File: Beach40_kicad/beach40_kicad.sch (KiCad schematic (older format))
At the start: 9 parts, among them T1 TRANSFO

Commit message: Some tinkering.
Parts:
- removed SMA_E1: RF IN, symbol SMA_EDGE
- added J1: SMA, SMA, symbol SMA
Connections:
- wire segments 22 -> 18
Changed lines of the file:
@@
 EESchema Schematic File Version 2
+LIBS:sma
 LIBS:power
 LIBS:device
@@
 LIBS:contrib
 LIBS:valves
-LIBS:sma_edge
 LIBS:beach40_kicad-cache
-EELAYER 25 0
+EELAYER 27 0
 EELAYER END
 $Descr A4 11693 8268
@@
 Sheet 1 1
 Title ""
-Date "19 jan 2015"
+Date "27 jan 2015"
 Rev ""
 Comp ""
@@
 Comment4 ""
 $EndDescr
-$Comp
-L SMA_EDGE SMA_E1
-U 1 1 54BB5708
-P 1650 5000
-F 0 "SMA_E1" H 1800 5300 60  0000 C CNN
-F 1 "RF IN" H 1800 5200 60  0000 C CNN
-F 2 "" H 1650 5000 60  0000 C CNN
-F 3 "" H 1650 5000 60  0000 C CNN
-	1    1650 5000
-	-1   0    0    1
-$EndComp
 $Comp
 L POT RV1
@@
 $EndComp
 Wire Wire Line
-	2000 5000 2100 5000
-Wire Wire Line
 	2500 5000 2650 5000
 $Comp
-L GND #PWR03
-U 1 1 54C61B84
-P 2100 5450
-F 0 "#PWR03" H 2100 5450 30  0001 C CNN
-F 1 "GND" H 2100 5380 30  0001 C CNN
-F 2 "" H 2100 5450 60  0000 C CNN
-F 3 "" H 2100 5450 60  0000 C CNN
-	1    2100 5450
-	1    0    0    -1
-$EndComp
-$Comp
-L GND #PWR04
-U 1 1 54C61BBC
-P 2050 4550
-F 0 "#PWR04" H 2050 4550 30  0001 C CNN
-F 1 "GND" H 2050 4480 30  0001 C CNN
-F 2 "" H 2050 4550 60  0000 C CNN
-F 3 "" H 2050 4550 60  0000 C CNN
-	1    2050 4550
-	1    0    0    -1
-$EndComp
-Wire Wire Line
-	2000 5100 2000 5450
-Wire Wire Line
-	2000 5450 2100 5450
-Wire Wire Line
-	2000 4900 2000 4550
-Wire Wire Line
-	2000 4550 2050 4550
+L SMA J1
+U 1 1 54C729C5
+P 1750 5300
+F 0 "J1" H 1875 5615 60  0000 C CNN
+F 1 "SMA" H 1940 5540 60  0000 C CNN
+F 2 "SMA" H 1925 5470 50  0000 C CNN
+F 3 "" H 1750 5300 60  0000 C CNN
+	1    1750 5300
+	-1   0    0    -1
+$EndComp
+Wire Wire Line
+	1900 5000 2100 5000
 $EndSCHEMATC

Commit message: 2 RF amp stages, first attempt at layout, 1206 for the most part.
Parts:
- removed C1: 10nF, symbol C
- removed RV1: 200, ~, symbol POT
- added C1: 10n, FT:1210_CAP, symbol CAP
- added C3, C5, C6, C7, C8, C9: 100n, FT:1210_CAP, symbol CAP
- added C4: 1n, FT:1210_CAP, symbol CAP
- added L1: 10T BiFilar, FT:IND_SRP1040, symbol INDUCTOR
- added L2, L3, L4: 10t BiFilar, FT:IND_SRP1040, symbol INDUCTOR
- added Q1: 2N2222, FT:SOT23_TRANSISTOR, symbol TRANSISTOR_NPN
- added Q2: BD139, FT:SOT23_TRANSISTOR, symbol TRANSISTOR_NPN
- added R1, R4: 100, FT:1206, symbol R
- added R2, R7: 2.2k, FT:1206, symbol R
- added R3: 1k1, FT:1206, symbol R
- added R5: 10, FT:1206, symbol R
- added R6: 470, FT:1206, symbol R
- added R8: 22, FT:1206, symbol R
- added R9: 4.7, FT:1206, symbol R
- added VR1: 200, FT:POT_TRIM_PTH, symbol POT
- 4:1: renamed from T1; symbol TRANSFO -> TRANSFORMER
- C2: footprint (none) -> FT:1210_CAP; symbol C -> CAP
- D1, D2, D3, D4: footprint ~ -> FT:1206_DIODE
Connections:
- net labels added: +12V, LPF
- wire segments 18 -> 63

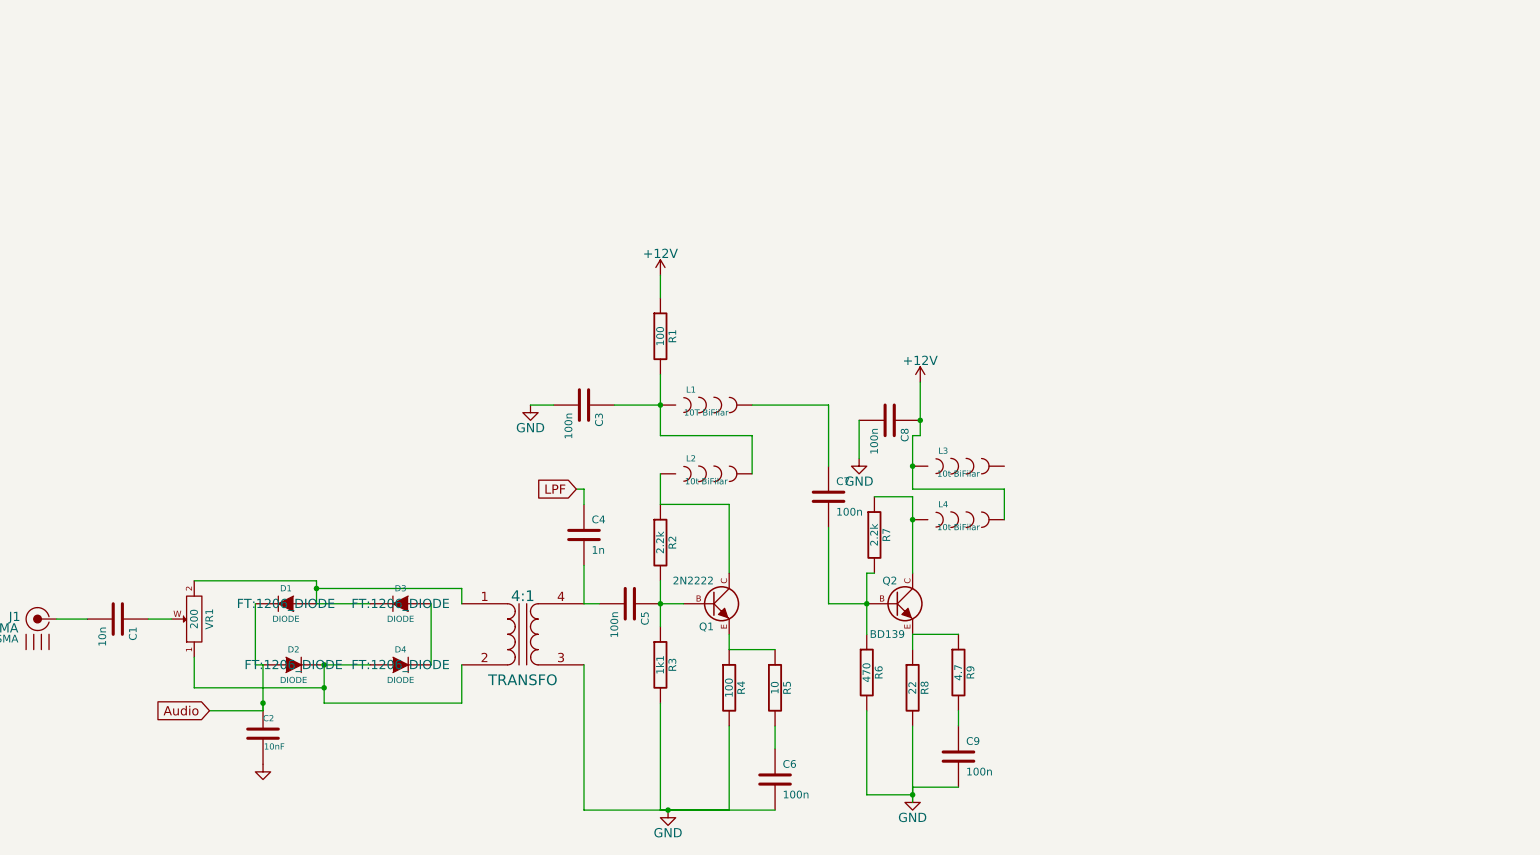
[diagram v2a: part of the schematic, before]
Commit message: - more work! transmit RF path finish.
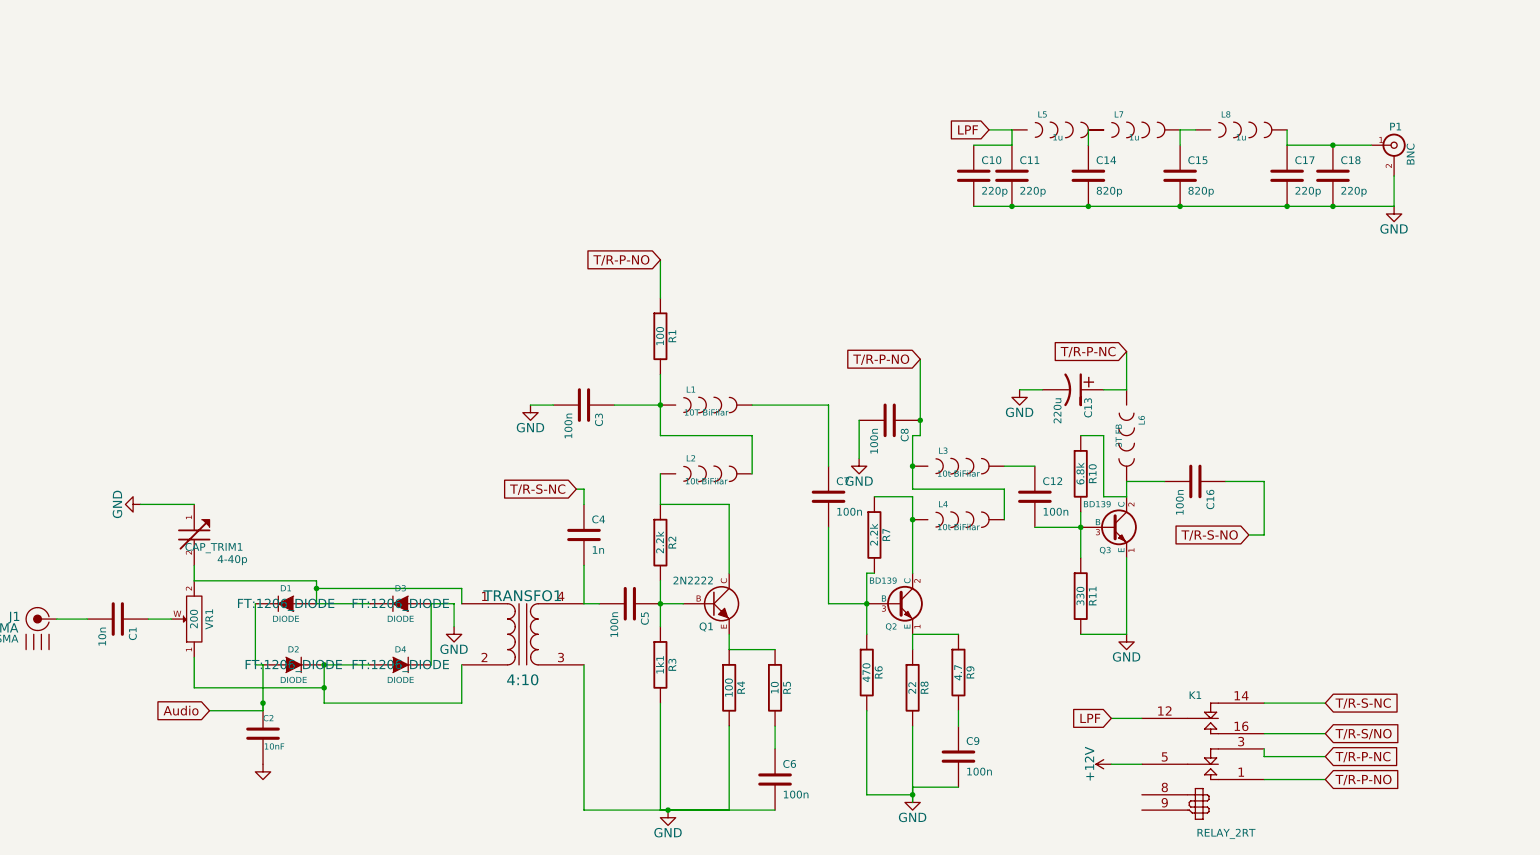
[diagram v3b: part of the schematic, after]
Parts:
- removed Q2: BD139, FT:SOT23_TRANSISTOR, symbol TRANSISTOR_NPN
- added C10, C11, C17, C18: 220p, symbol CAP
- added C12, C16: 100n, symbol CAP
- added C13: 220u, symbol C_POL
- added C14, C15: 820p, symbol CAP
- added CAP_TRIM1: 4-40p, symbol CAP_TRIM
- added K1: RELAY_2RT, symbol RELAY_2RT
- added L5, L7, L8: 1u, symbol INDUCTOR
- added L6: 3T FB, symbol INDUCTOR
- added P1: BNC, symbol BNC
- added Q2: BD139, FT:SOT23_TRANSISTOR, symbol BD139
- added Q3: BD139, TO126, symbol BD139
- added R10: 6.8k, symbol R
- added R11: 330, symbol R
- TRANSFO1: renamed from 4:1; value TRANSFO -> 4:10
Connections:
- net +12V: now also K1.5 (C1); no longer C8.1, L3.1, L4.2, R1.1
- net GND: now also D3.A, D4.K, C10.2, C11.2, C13.2 (-), C14.2, C15.2, C17.2, C18.2, CAP_TRIM1.1, P1.2 (Ext), Q3.1 (E), R11.2
- net LPF: now also C10.1, C11.1, K1.12 (C2), L5.1; no longer C4.1
- net at D1.A, D3.K, TRANSFO1.1 (AA)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: now also CAP_TRIM1.2
- net at C7.2, R6.1, R7.2: now also Q2.3 (B)
- net at L4.1, R7.1: now also Q2.2 (C)
- net at R8.1, R9.1: now also Q2.1 (E)
- net at L3.2: now also C12.1
- new net: C12.2, Q3.3 (B), R10.2, R11.1
- new net: C16.2, L6.2, Q3.2 (C), R10.1
- new net: C14.1, L7.1
- new net: C15.1, L7.2, L8.1
- new net: C17.1, C18.1, L8.2, P1.1 (In)
- new net T/R-P-NC: C13.1 (+), K1.3 (R1), L6.1
- new net T/R-P-NO: C8.1, K1.1 (T1), L3.1, L4.2, R1.1
- new net T/R-S-NC: C4.1, K1.14 (R2)
- new net T/R-S-NO: C16.1
- new net T/R-S/NO: K1.16 (T2)

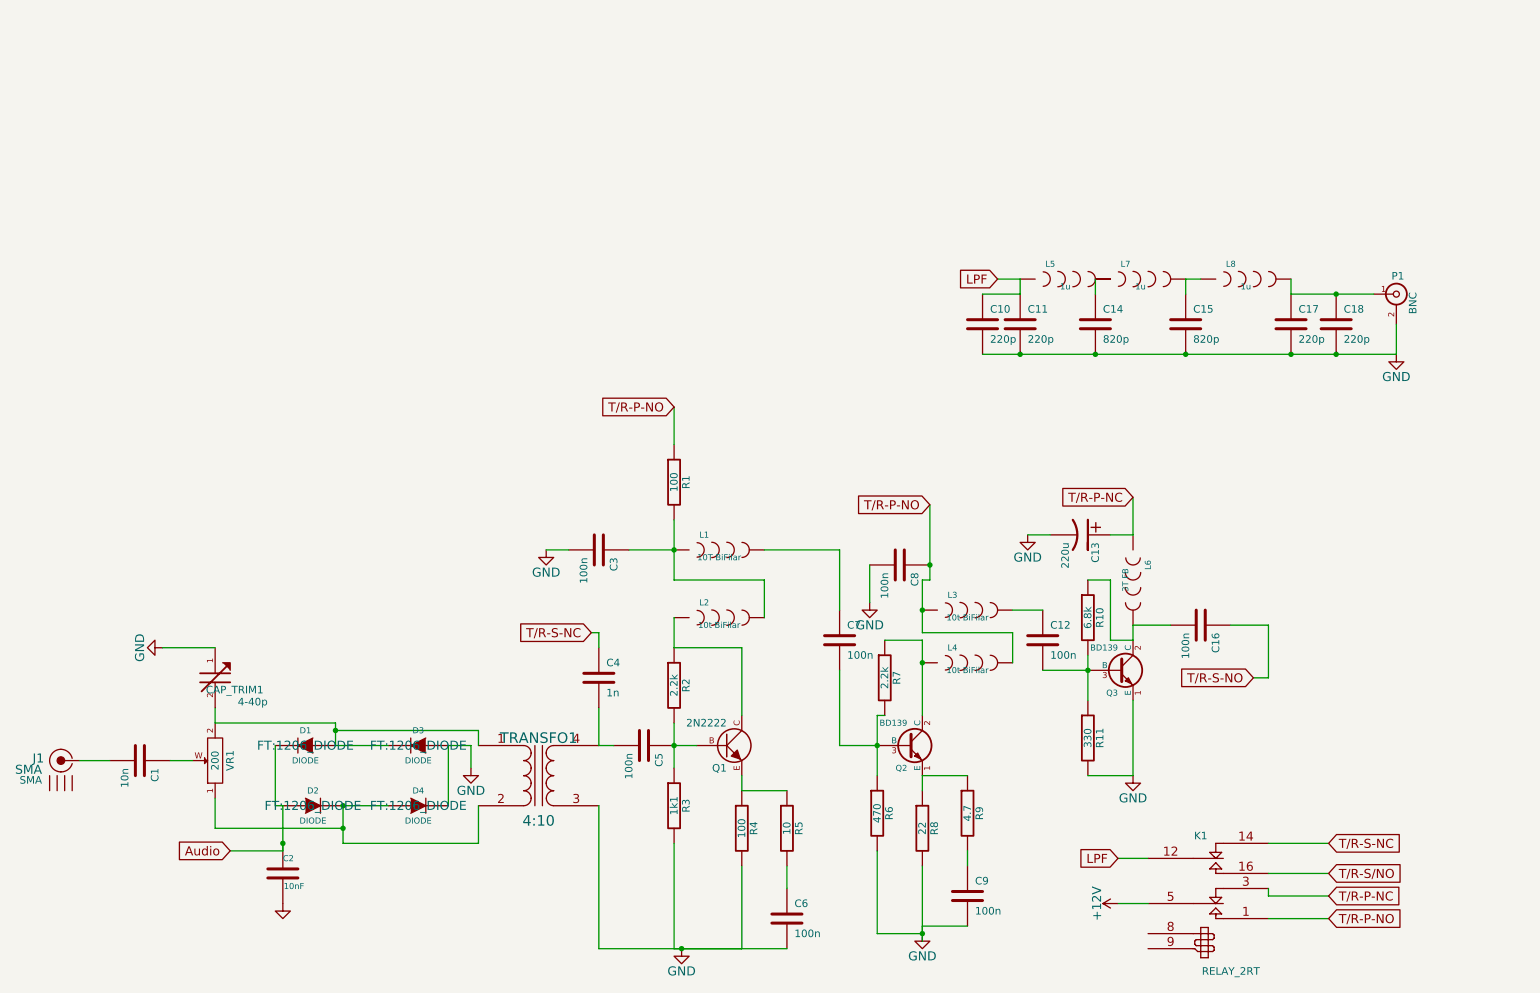
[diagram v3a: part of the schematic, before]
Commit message: All components on schematic, working out libraries.
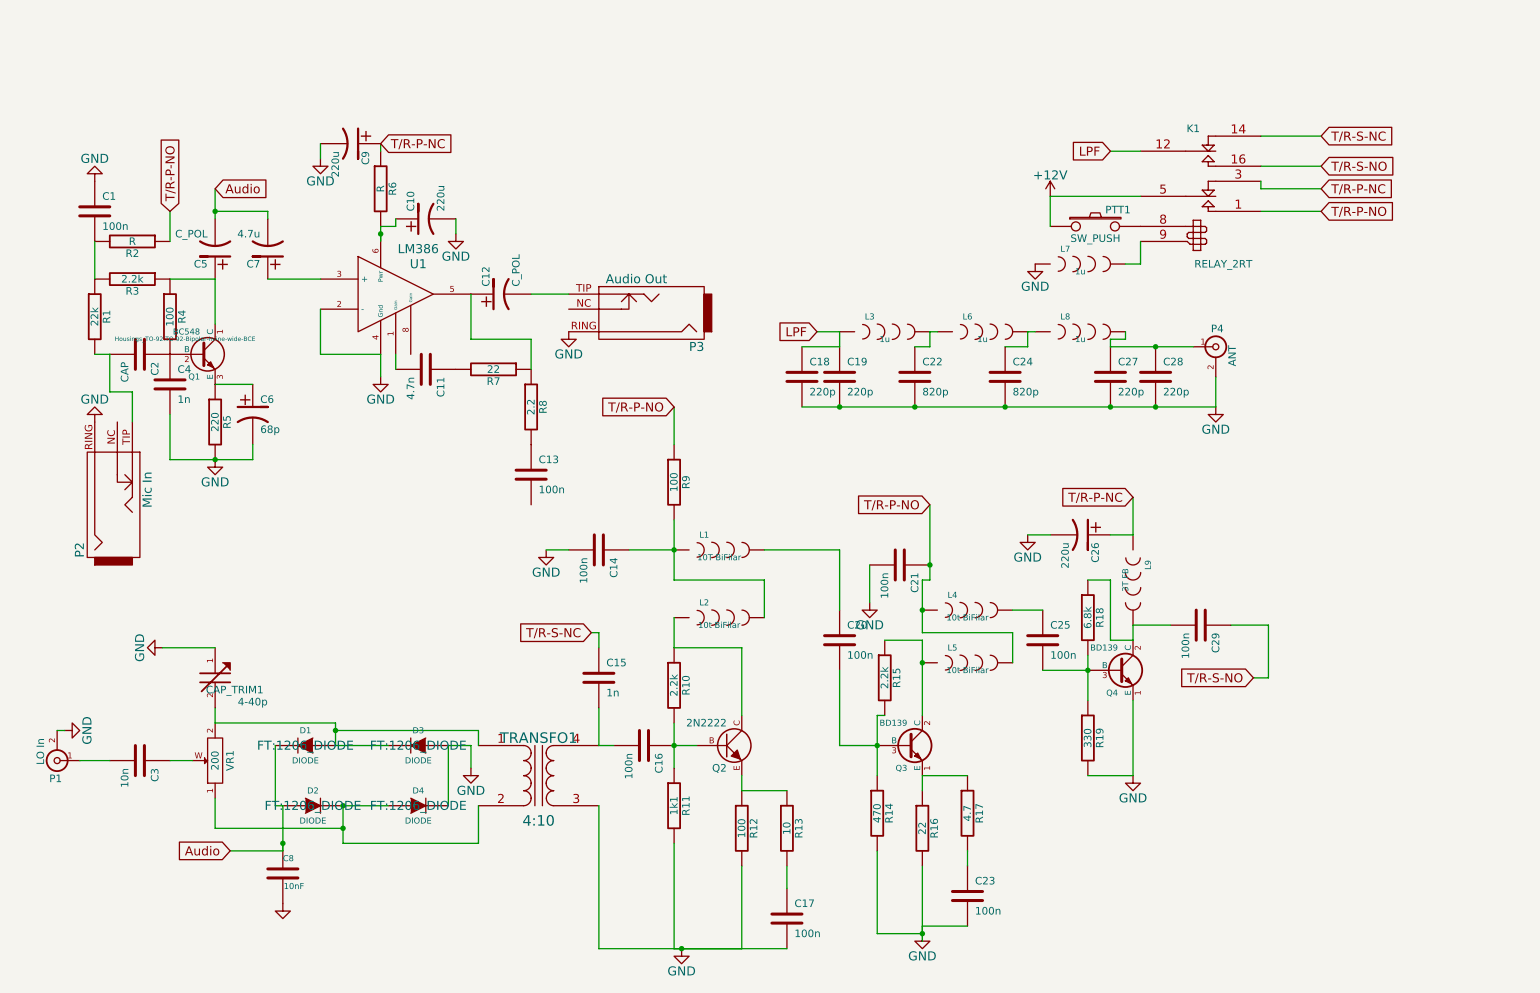
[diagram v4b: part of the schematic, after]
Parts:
- removed J1: SMA, SMA, symbol SMA
- added C1: 100n, FT:1210_CAP, symbol CAP
- added C10: 220u, symbol C_POL
- added C11: 4.7n, symbol CAP
- added C12: C_POL, symbol C_POL
- added C13: 100n, symbol CAP
- added C2: CAP, FT:1210_CAP, symbol CAP
- added C4: 1n, FT:1210_CAP, symbol CAP
- added C5: C_POL, FT:CAP_ELECTRO_D4S1.8, symbol C_POL
- added C6: 68p, FT:CAP_ELECTRO_D4S1.8, symbol C_POL
- added C7: 4.7u, FT:1210_CAP, symbol C_POL
- added C9: 220u, FT:1210_CAP, symbol C_POL
- added L7: 1u, Choke_Axial_ThroughHole:Choke_Horizontal_RM15mm, symbol INDUCTOR
- added P1: LO In, Sockets_BNC:BNC_Socket_TYCO-AMP_LargePads, symbol BNC
- added P2: Mic In, symbol CON_JACK_MONO_SW
- added P3: Audio Out, symbol CON_JACK_MONO_SW
- added PTT1: SW_PUSH, symbol SW_PUSH
- added Q1: BC548, Housings_TO-92:TO-92-Bipolar-inline-wide-BCE, symbol BC548
- added R1: 22k, FT:RES_AXIAL_400MIL, symbol R
- added R2, R6: R, FT:RES_AXIAL_400MIL, symbol R
- added R3: 2.2k, FT:RES_AXIAL_400MIL, symbol R
- added R4: 100, FT:RES_AXIAL_400MIL, symbol R
- added R5: 220, FT:RES_AXIAL_400MIL, symbol R
- added R7: 22, FT:RES_AXIAL_400MIL, symbol R
- added R8: 2.2, FT:RES_AXIAL_400MIL, symbol R
- added U1: LM386, symbol LM386
- C14: renamed from C3; footprint FT:1210_CAP -> (none)
- C15: renamed from C4; footprint FT:1210_CAP -> (none)
- C16: renamed from C5; footprint FT:1210_CAP -> (none)
- C17: renamed from C6; footprint FT:1210_CAP -> (none)
- K1: footprint (none) -> Relays_ThroughHole:Relais_DPDT_Schrack-RT2_RM5mm
- L3: renamed from L5; footprint (none) -> Choke_Axial_ThroughHole:Choke_Horizontal_RM15mm
- L6: renamed from L7; footprint (none) -> Choke_Axial_ThroughHole:Choke_Horizontal_RM15mm
- L8: footprint (none) -> Choke_Axial_ThroughHole:Choke_Horizontal_RM15mm
- L9: renamed from L6; footprint (none) -> FT:IND_SRP1040
- P4: renamed from P1; value BNC -> ANT; footprint (none) -> Sockets_BNC:BNC_Socket_TYCO-AMP_LargePads
- Q2: renamed from Q1; footprint FT:SOT23_TRANSISTOR -> Housings_TO-92:TO-92-Bipolar-inline-wide-BCE
- Q3: renamed from Q2; footprint FT:SOT23_TRANSISTOR -> Transistors_TO-220:TO-220_Bipolar-BCE_Vertical_LargePads
- Q4: renamed from Q3; footprint TO126 -> Transistors_TO-220:TO-220_Bipolar-BCE_Vertical_LargePads
- R10: renamed from R2; footprint FT:1206 -> FT:RES_AXIAL_400MIL
- R11: renamed from R3; footprint FT:1206 -> FT:RES_AXIAL_400MIL
- R12: renamed from R4; footprint FT:1206 -> FT:RES_AXIAL_400MIL
- R13: renamed from R5; footprint FT:1206 -> FT:RES_AXIAL_400MIL
- R14: renamed from R6; footprint FT:1206 -> FT:RES_AXIAL_400MIL
- R15: renamed from R7; footprint FT:1206 -> FT:RES_AXIAL_400MIL
- R16: renamed from R8; footprint FT:1206 -> FT:RES_AXIAL_400MIL
- R17: renamed from R9; footprint FT:1206 -> FT:RES_AXIAL_400MIL
- R18: renamed from R10; footprint (none) -> FT:RES_AXIAL_400MIL
- R19: renamed from R11; footprint (none) -> FT:RES_AXIAL_400MIL
- R9: renamed from R1; footprint FT:1206 -> FT:RES_AXIAL_400MIL
- renumbered C10 to C18, C11 to C19, C7 to C20, C8 to C21, C14 to C22, C9 to C23, C15 to C24, C12 to C25, C13 to C26, C17 to C27, C18 to C28, C16 to C29, C1 to C3, C2 to C8, L3 to L4, L4 to L5
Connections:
- net T/R-S/NO is gone; now on net T/R-S-NO: K1.16 (T2)
- net +12V: now also PTT1.1
- net Audio: now also C5.2 (-), C7.2 (-)
- net GND: now also C1.1, C10.2 (-), C4.2, C6.2 (-), C9.2 (-), L7.1, P1.2 (Ext), P2.RING, P3.RING, R5.2, U1.2 (-), U1.4 (Gnd)
- net T/R-P-NC: now also C9.1 (+), R6.1
- net T/R-P-NO: now also R2.1
- net at C3.2: now also P1.1 (In)
- net at K1.8: now also PTT1.2
- net at K1.9: now also L7.2
- net at L3.2: now also C22.1, L6.1
- new net: C7.1 (+), U1.3 (+)
- new net: C11.2, U1.1 (Gain)
- new net: C12.1 (+), R7.1, R8.1, U1.5
- new net: C10.1 (+), R6.2, U1.6 (Pwr)
- new net: C11.1, R7.2
- new net: C13.1, R8.2
- new net: C12.2 (-), P3.TIP
- new net: C5.1 (+), Q1.1 (C), R3.1, R4.1
- new net: C2.1, C4.1, Q1.2 (B), R4.2
- new net: C6.1 (+), Q1.3 (E), R5.1
- new net: C1.2, R1.1, R2.2, R3.2
- new net: C2.2, P2.TIP, R1.2
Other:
- moved on the sheet: C18, C19, C22, C24, C27, C28, K1, L3, L6, L8, P4
